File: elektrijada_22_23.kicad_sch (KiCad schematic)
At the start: 172 parts

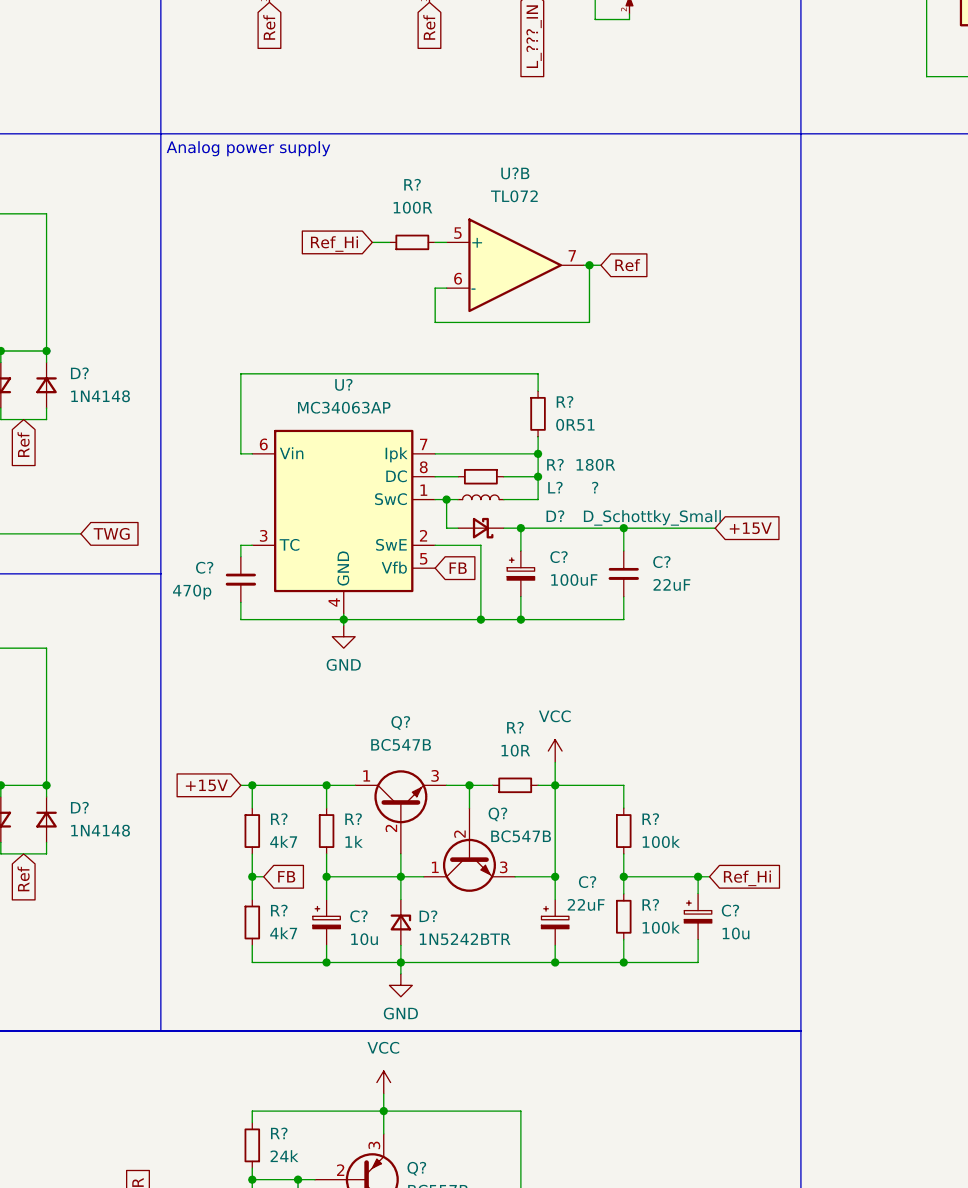
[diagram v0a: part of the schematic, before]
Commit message: Chore: added LT1618 symbol and changed buck boost design
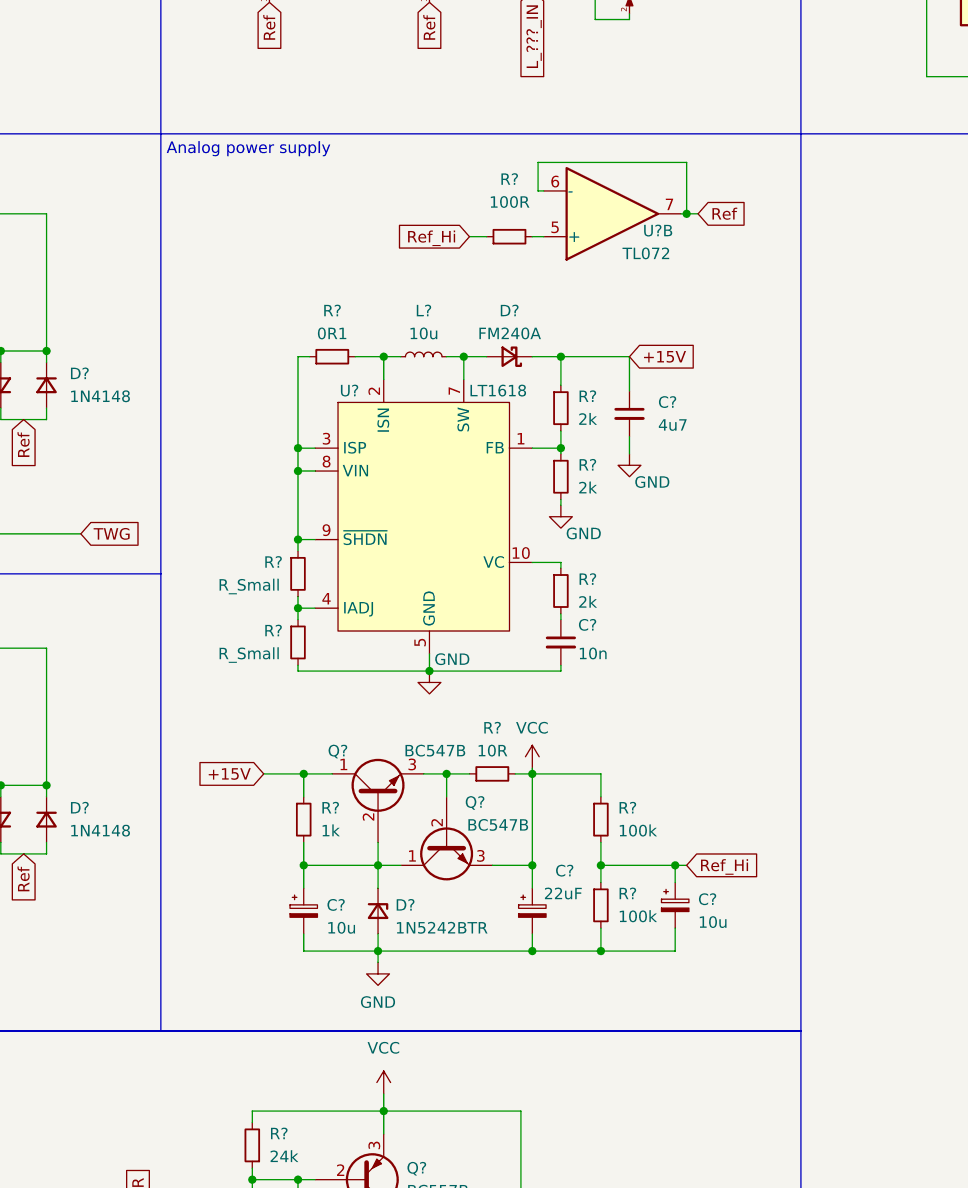
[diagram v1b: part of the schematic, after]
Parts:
- removed C?: 470p, symbol Device:C_Small
- removed C?: 100uF, symbol Device:C_Polarized_Small
- removed C?: 22uF, symbol Device:C_Small
- removed D?: D_Schottky_Small, symbol Device:D_Schottky_Small
- removed L?: ?, symbol Device:L_Small
- removed R?: 0R51, symbol Device:R_Small
- removed R? (x2): 4k7, symbol Device:R_Small
- removed R?: 180R, symbol Device:R_Small
- removed U?: MC34063AP, Package_DIP:DIP-8_W7.62mm, symbol Regulator_Switching:MC34063AP
- added C?: 10n, symbol Device:C_Small
- added C?: 4u7, symbol Device:C_Small
- added D?: FM240A, symbol Device:D_Schottky_Small
- added L?: 10u, symbol Device:L_Small
- added R? (x3): 2k, symbol Device:R_Small
- added R? (x2): R_Small, symbol Device:R_Small
- added R?: 0R1, symbol Device:R_Small
- added U?: LT1618, symbol LT1618:LT1618
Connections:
- net +15V: now also C?.1, D?.1 (K), R?.1
- net GND: now also C?.2, C?.2, R?.2, R?.2, U?.5 (GND)
- new net: C?.1, R?.2
- new net: R?.1, U?.10 (VC)
- new net: R?.1, R?.1, U?.3 (ISP), U?.8 (VIN), U?.9 (~{SHDN})
- new net: R?.1, R?.2, U?.4 (IADJ)
- new net: R?.1, R?.2, U?.1 (FB)
- new net: L?.1, R?.2, U?.2 (ISN)
- new net: D?.2 (A), L?.2, U?.7 (SW)
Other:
- moved on the sheet: C?, D?, Q?, R?, U?B
